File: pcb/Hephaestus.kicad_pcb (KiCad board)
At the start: 4 copper layers, 70 x 25 mm, 97 parts, among them J1 Fottpedal, J2 BT_ACTION, J3 USB_C_Receptacle_USB2.0, J4 PROG_CONN, J5 DBG_UART, J6 LED_CONN, M1 28BYJ-48 (5V), Q1 AON7414, SW1 OLED_<, SW2 OLED_#, SW3 OLED_>, SW4 BT_RESET, U1 74HC14, U2 USBLC6-2SC6, U3 NCV8165ML330, U4 STM32L432KCUx, U5 M24C32, U6 OLED-128x32, U7 KTD2026BEWE, U8 MIC2288, U9 STSPIN820

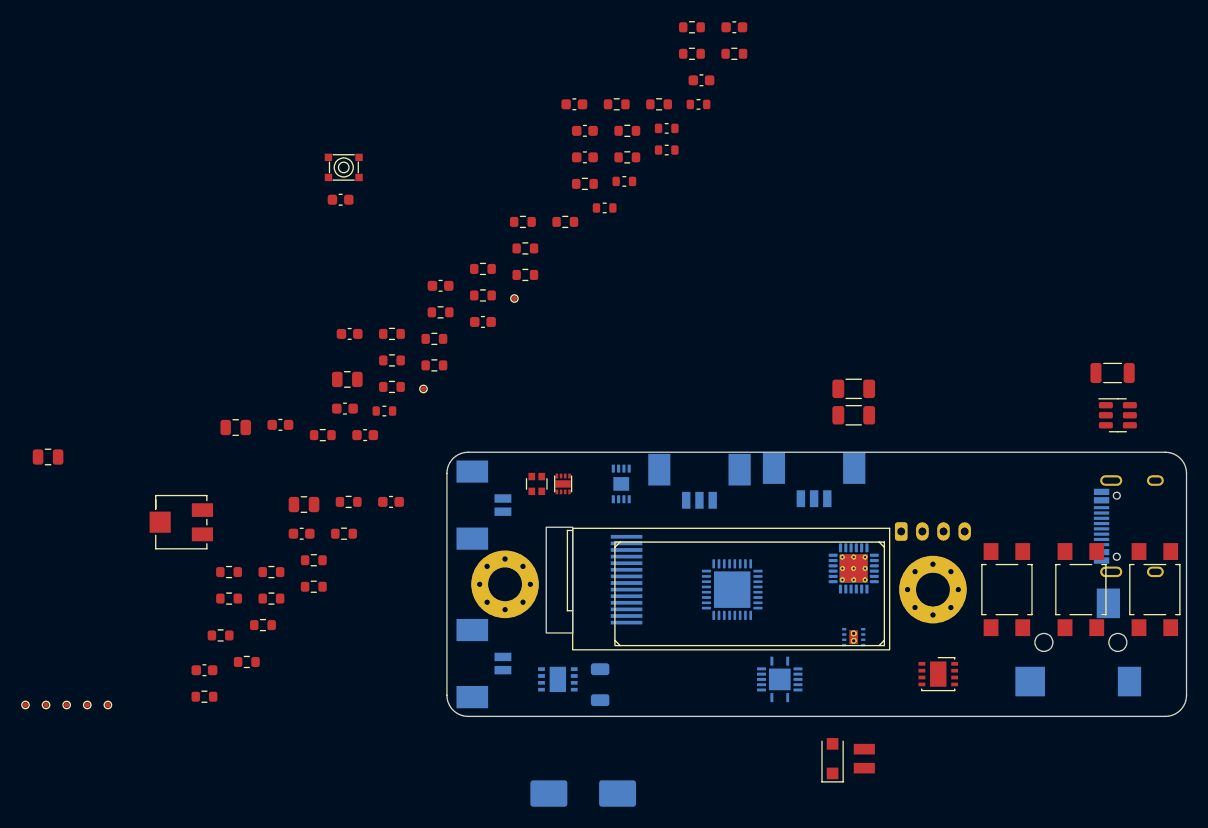
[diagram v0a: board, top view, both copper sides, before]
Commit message: PCB: Basic routing done
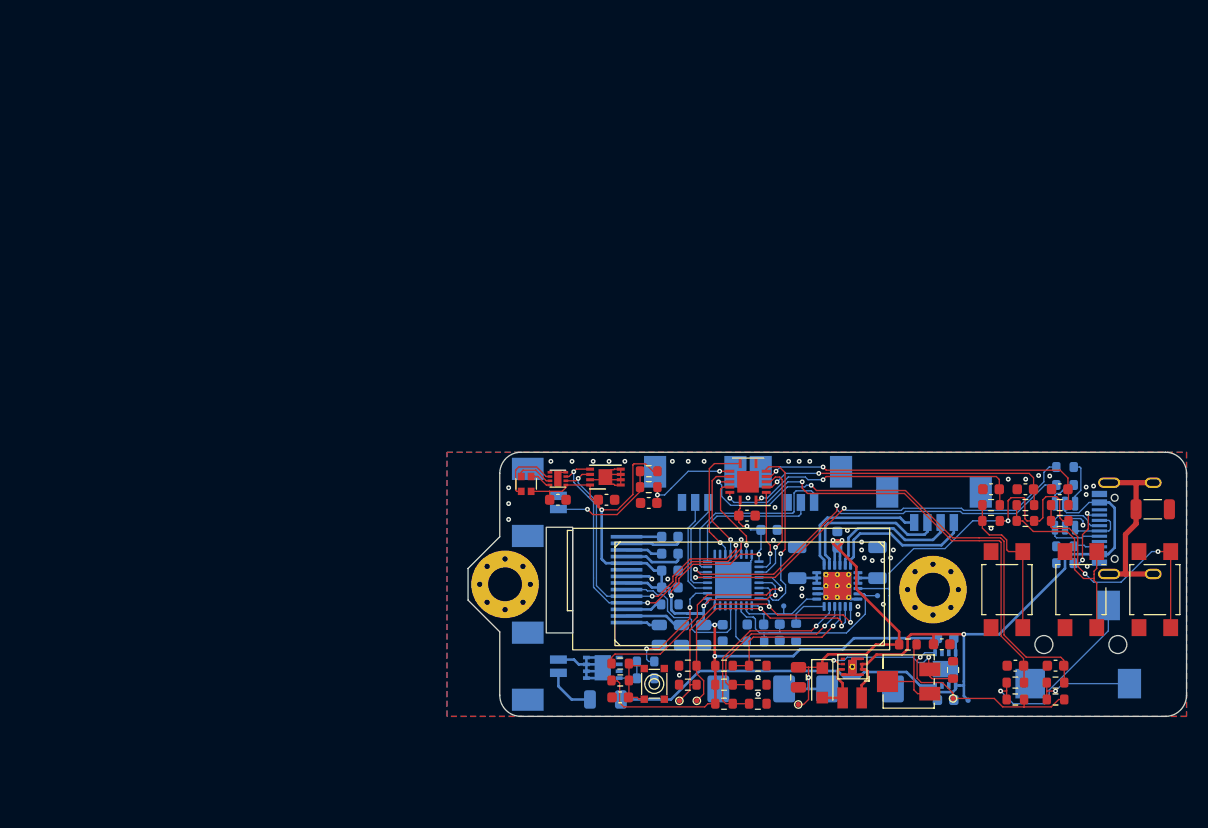
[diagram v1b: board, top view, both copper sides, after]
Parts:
- added C27: 100nF, Capacitor_SMD:C_0603_1608Metric, B.Cu at (164.2, 121.3)
- added C28: 100uF/16V, Capacitor_Tantalum_SMD:CP_EIA-7343-30_AVX-N, B.Cu at (163.8, 127.4)
- C1, C2, C3, C4, C5, C6: footprint TCY_passives:C_0603_1608Metric -> Capacitor_SMD:C_0603_1608Metric
- C10, C11, C12, C13, C15, C16, C17, C19, C20, C21, C25, C26, C9, R13, R14, R15, R16, R19, R20, R22, R31, R34, R35, R36, TP1, TP4, TP5, U2, U3: moved to B.Cu
- C24: value 330uF -> 100uF/16V; footprint Capacitor_SMD:CP_Elec_8x10 -> Capacitor_Tantalum_SMD:CP_EIA-7343-30_AVX-N
- J1: value Fottpedal -> Footpedal
- M1: footprint Connector_JST:JST_PH_S4B-PH-K_1x04_P2.00mm_Horizontal -> TCY_connectors:Amphenol_10114830-11103LF_1x04_P1.25mm_Horizontal
- U1, U5, U8: moved to F.Cu
- moved TP4 79.4 mm to (175.8, 118.6), turned to 180 degrees
- moved RV1 70.5 mm to (178.7, 126.7)
- moved R9 69.6 mm to (188.8, 126.8)
- moved R3 69.4 mm to (192.6, 128.4), turned to 180 degrees
- moved TP5 68.5 mm to (166.9, 119.5), turned to 180 degrees
- moved C9 68.1 mm to (182.2, 128.4)
- moved C2 67.9 mm to (192.6, 125.2), turned to 180 degrees
- moved R1 66.6 mm to (188.8, 128.4), turned to 180 degrees
- moved R8 66.0 mm to (192.6, 126.8)
- moved TP3 65.3 mm to (168.2, 128.9)
- moved R16 65.3 mm to (193.5, 108.1), turned to 180 degrees
- moved R23 65.1 mm to (178.6, 123.2)
- moved TP6 63.5 mm to (158.7, 128.5)
- moved R13 63.4 mm to (193.5, 115.5), turned to 180 degrees
- moved C16 62.3 mm to (157.2, 122.3), turned to -90 degrees
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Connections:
- J2 pad 1: GND -> Net-(R2-Pad2)
- J2 pad 2: Net-(J2-Pad2) -> GND
- M1 pad 1: Net-(M1-Pad1) -> Net-(U9-Pad7)
- M1 pad 2: Net-(M1-Pad2) -> Net-(U9-Pad8)
- M1 pad 3: Net-(M1-Pad3) -> Net-(U9-Pad11)
- M1 pad 4: Net-(M1-Pad4) -> Net-(U9-Pad12)
- R2 pad 2: Net-(J2-Pad2) -> Net-(R2-Pad2)
- R7 pad 1: Net-(J2-Pad2) -> Net-(R2-Pad2)
- U1 pad 1: Net-(C1-Pad1) -> Net-(C4-Pad1)
- U1 pad 10: /BT_OLED_# -> /BT_PEDAL1
- U1 pad 11: Net-(C5-Pad1) -> Net-(C2-Pad1)
- U1 pad 12: /BT_OLED_> -> /BT_PEDAL2
- U1 pad 13: Net-(C6-Pad1) -> Net-(C3-Pad1)
- U1 pad 2: /BT_ACTION -> /BT_OLED_<
- U1 pad 3: Net-(C2-Pad1) -> Net-(C5-Pad1)
- U1 pad 4: /BT_PEDAL1 -> /BT_OLED_#
- U1 pad 5: Net-(C3-Pad1) -> Net-(C6-Pad1)
- U1 pad 6: /BT_PEDAL2 -> /BT_OLED_>
- U1 pad 8: /BT_OLED_< -> /BT_ACTION
- U1 pad 9: Net-(C4-Pad1) -> Net-(C1-Pad1)
- U4 pad 2: /BT_OLED_# -> /BT_OLED_<
- U4 pad 27: /BT_PEDAL2 -> /BT_ACTION
- U4 pad 3: /BT_OLED_< -> /BT_OLED_#
- U4 pad 31: /BT_OLED_> -> /BT_PEDAL2
- U4 pad 6: /BT_ACTION -> /BT_OLED_>
- U9 pad 11: Net-(M1-Pad4) -> Net-(U9-Pad11)
- U9 pad 12: Net-(M1-Pad3) -> Net-(U9-Pad12)
- U9 pad 7: Net-(M1-Pad2) -> Net-(U9-Pad7)
- U9 pad 8: Net-(M1-Pad1) -> Net-(U9-Pad8)
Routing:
- net +3V3: track 0.00 -> 174.4 mm, vias 0 -> 10
- net VBUS: track 0.00 -> 87.3 mm, vias 0 -> 1
- net Net-(C2-Pad1): track 0.00 -> 50.3 mm, vias 0 -> 2
- net Net-(C3-Pad1): track 0.00 -> 44.1 mm, vias 0 -> 2
- net /D-: track 0.00 -> 40.5 mm, vias 0 -> 2
- net /D+: track 0.00 -> 40.4 mm, vias 0 -> 2
- net +12V: track 0.00 -> 40.1 mm, vias 0 -> 3
- net GND: track 0.00 -> 37.3 mm, vias 0 -> 45
- net /SDA: track 0.00 -> 33.4 mm, vias 0 -> 3
- net Net-(C6-Pad1): track 0.00 -> 31.9 mm, vias 0 -> 2
- net /SCL: track 0.00 -> 30.3 mm, vias 0 -> 3
- net Net-(C5-Pad1): track 0.00 -> 28.6 mm, vias 0 -> 2
- net /MOT_STEP: track 0.00 -> 27.7 mm, vias 0 -> 2
- net Net-(C4-Pad1): track 0.00 -> 26.7 mm, vias 0 -> 2
- net /MOT_DIR: track 0.00 -> 25.8 mm, vias 0 -> 2
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- added copper zone on B.Cu, net GND
- added copper zone on F.Cu, net GND
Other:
- board size 70 x 25 mm -> 68 x 25 mm
- copper layers 4 -> 2

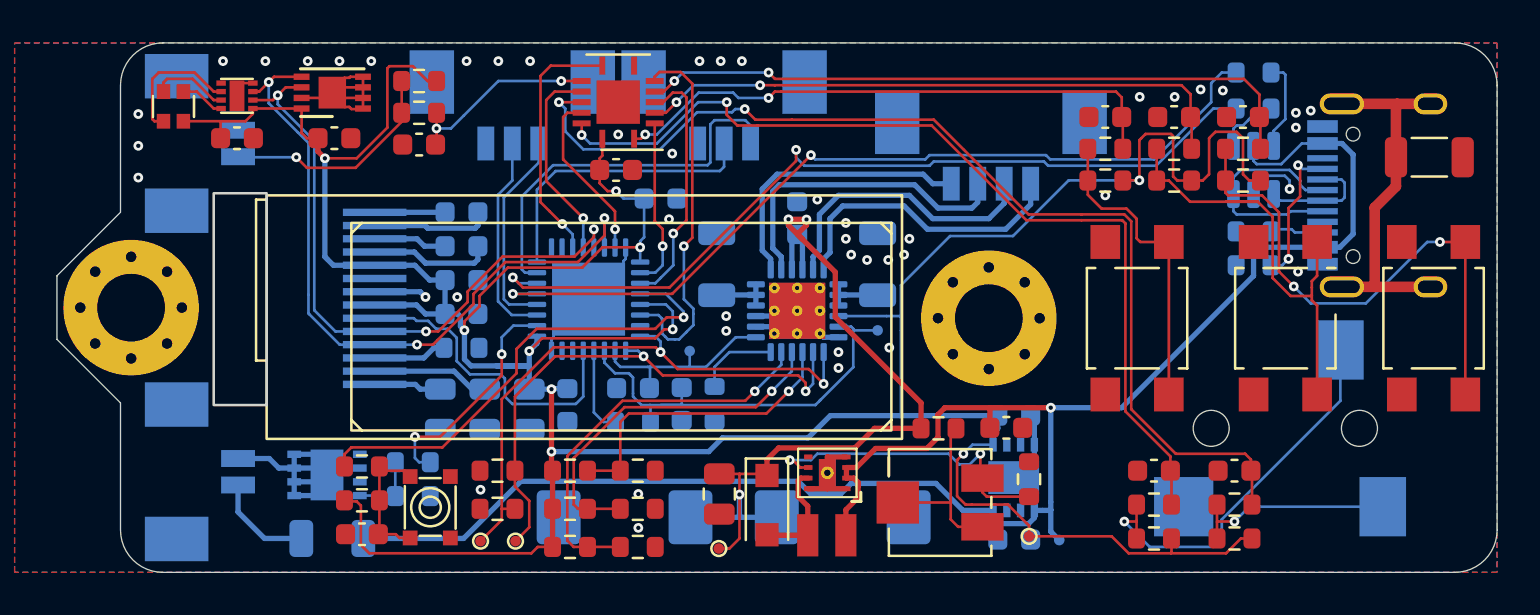
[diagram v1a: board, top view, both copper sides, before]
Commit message: PCB: add silkscreen marking
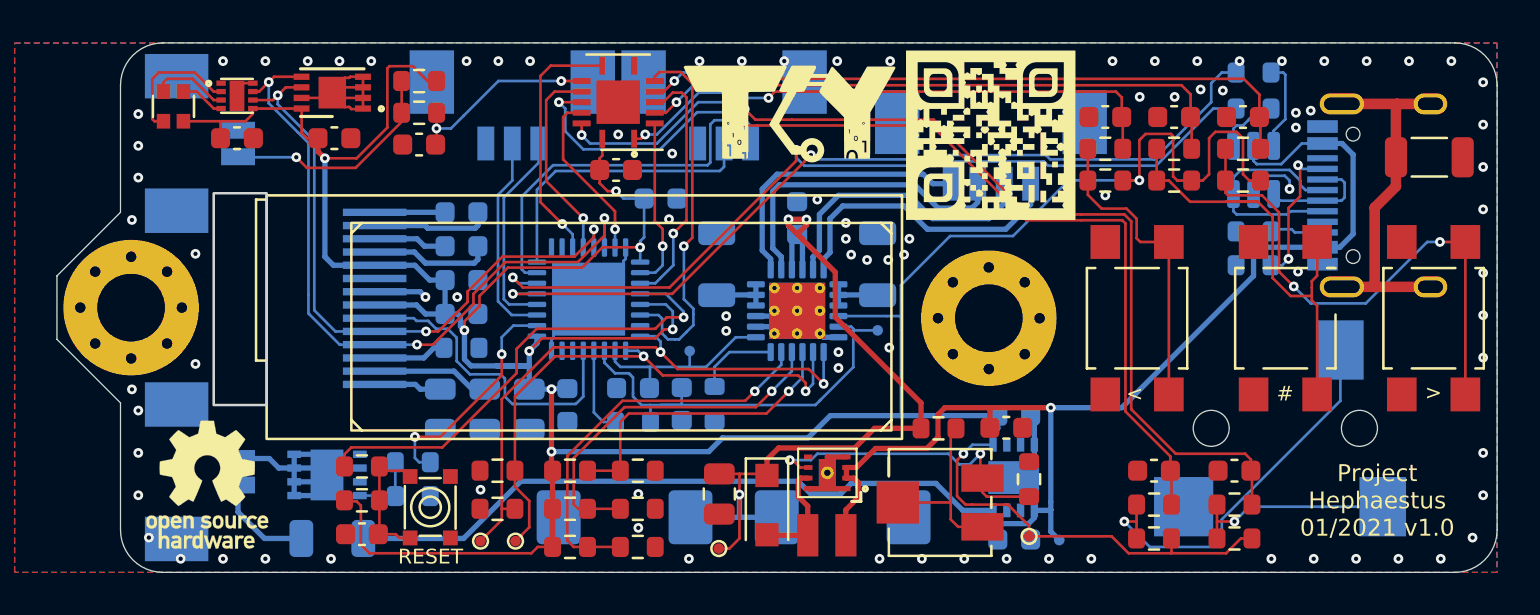
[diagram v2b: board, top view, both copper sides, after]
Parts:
- added G***: LOGO, LOGO, F.Cu at (171.6, 108.4)
- added G***: LOGO, LOGO, F.Cu at (181.1, 109.4)
- added REF**: OSHW-Logo_5.7x6mm_SilkScreen, Symbol:OSHW-Logo_5.7x6mm_SilkScreen, F.Cu at (144.1, 125.9)
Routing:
- net GND: vias 45 -> 90
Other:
- board text added: "#"
- board text added: "+"
- board text added: "-"
- board text added: "<"
- board text added: ">"
- board text added: "A1"
- board text added: "A2"
- board text added: "ACTION"
- board text added: "B1"
- board text added: "B2"
- board text added: "DRX"
- board text added: "DTX"
- board text added: "GND"
- board text added: "LED"
- board text added: "P1"
- board text added: "P2"
- board text added: "Pedal switch"
- board text added: "Project Hephaestus 01/2021 v1.0"
- board text added: "RESET"
- board text added: "SWC"
- board text added: "SWI"
- board text added: "TheColonelYoung@GitHub.com"
